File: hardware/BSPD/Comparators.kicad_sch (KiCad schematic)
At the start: 17 parts, among them U6 LM393, U7 LM393, U8 LM393, U9 74AHC1G32

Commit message: Crumbs of documentation added
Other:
- note added: "0.45V Out"
- note added: "Any voltage you desire out"
- note added: "Both comparators are set to detect braking within =< 30bar threshold; copied from previous BSPD Board"

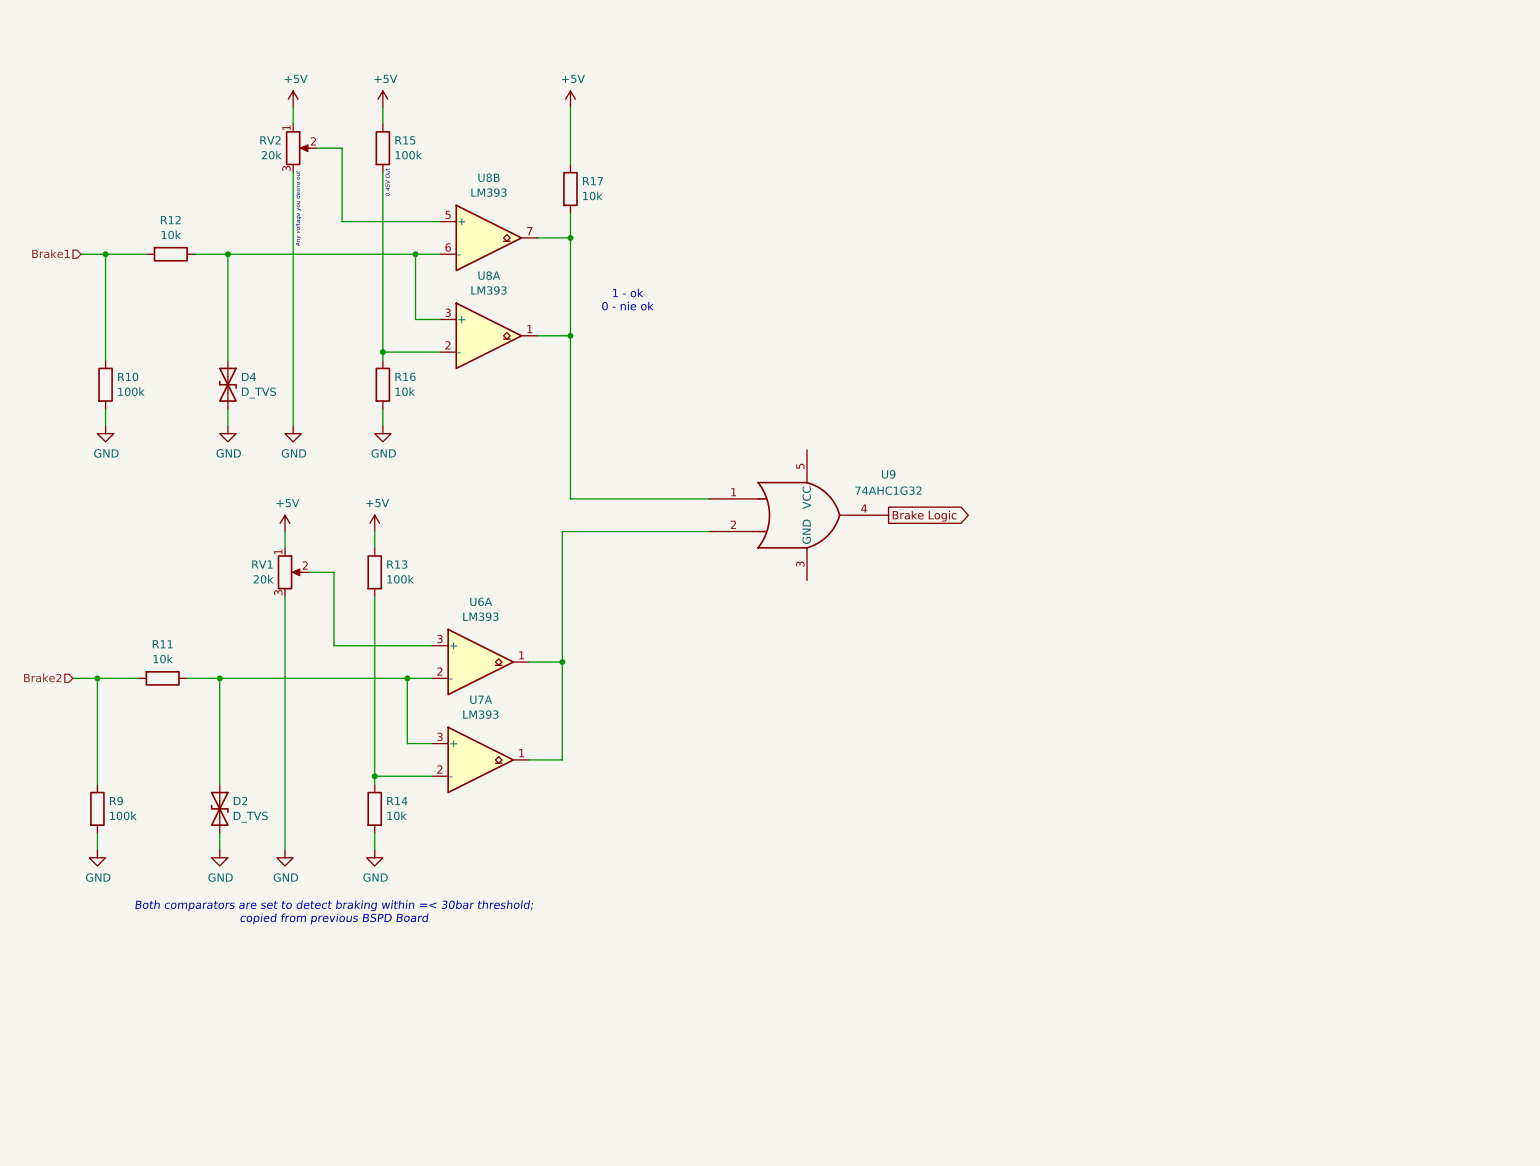
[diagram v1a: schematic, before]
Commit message: Timing Changed + Documented
Changed 10 second autoreset timer to a 555 in one-shot configuration. Also documented BSPD Board.
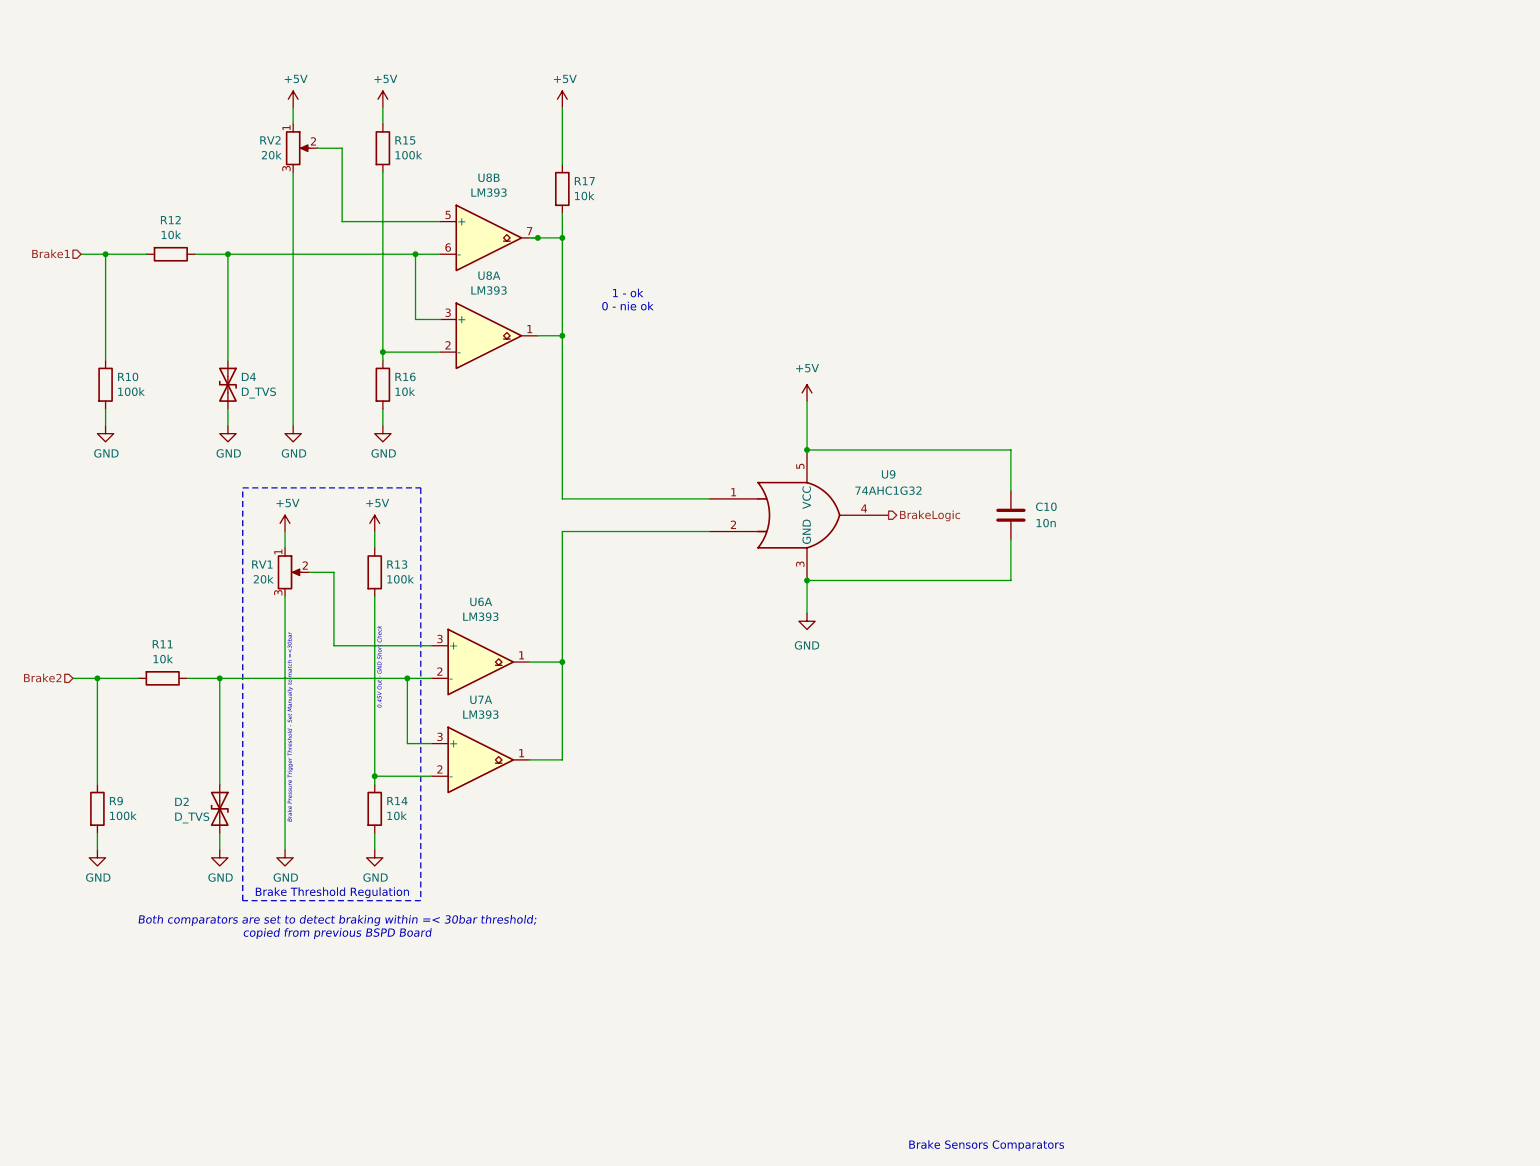
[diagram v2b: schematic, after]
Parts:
- added C10: 10n, symbol Device:C
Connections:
- net +5V: now also U9.5 (VCC), C10.1
- net GND: now also U9.3 (GND), C10.2
- net Brake Logic renamed BrakeLogic
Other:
- note added: "0.45V Out - GND Short Check"
- note added: "Brake Pressure Trigger Threshold - Set Manually to match =<30bar"
- note added: "Brake Sensors Comparators"
- note added: "Brake Threshold Regulation"
- note removed: "0.45V Out"
- note removed: "Any voltage you desire out"
- moved on the sheet: R17

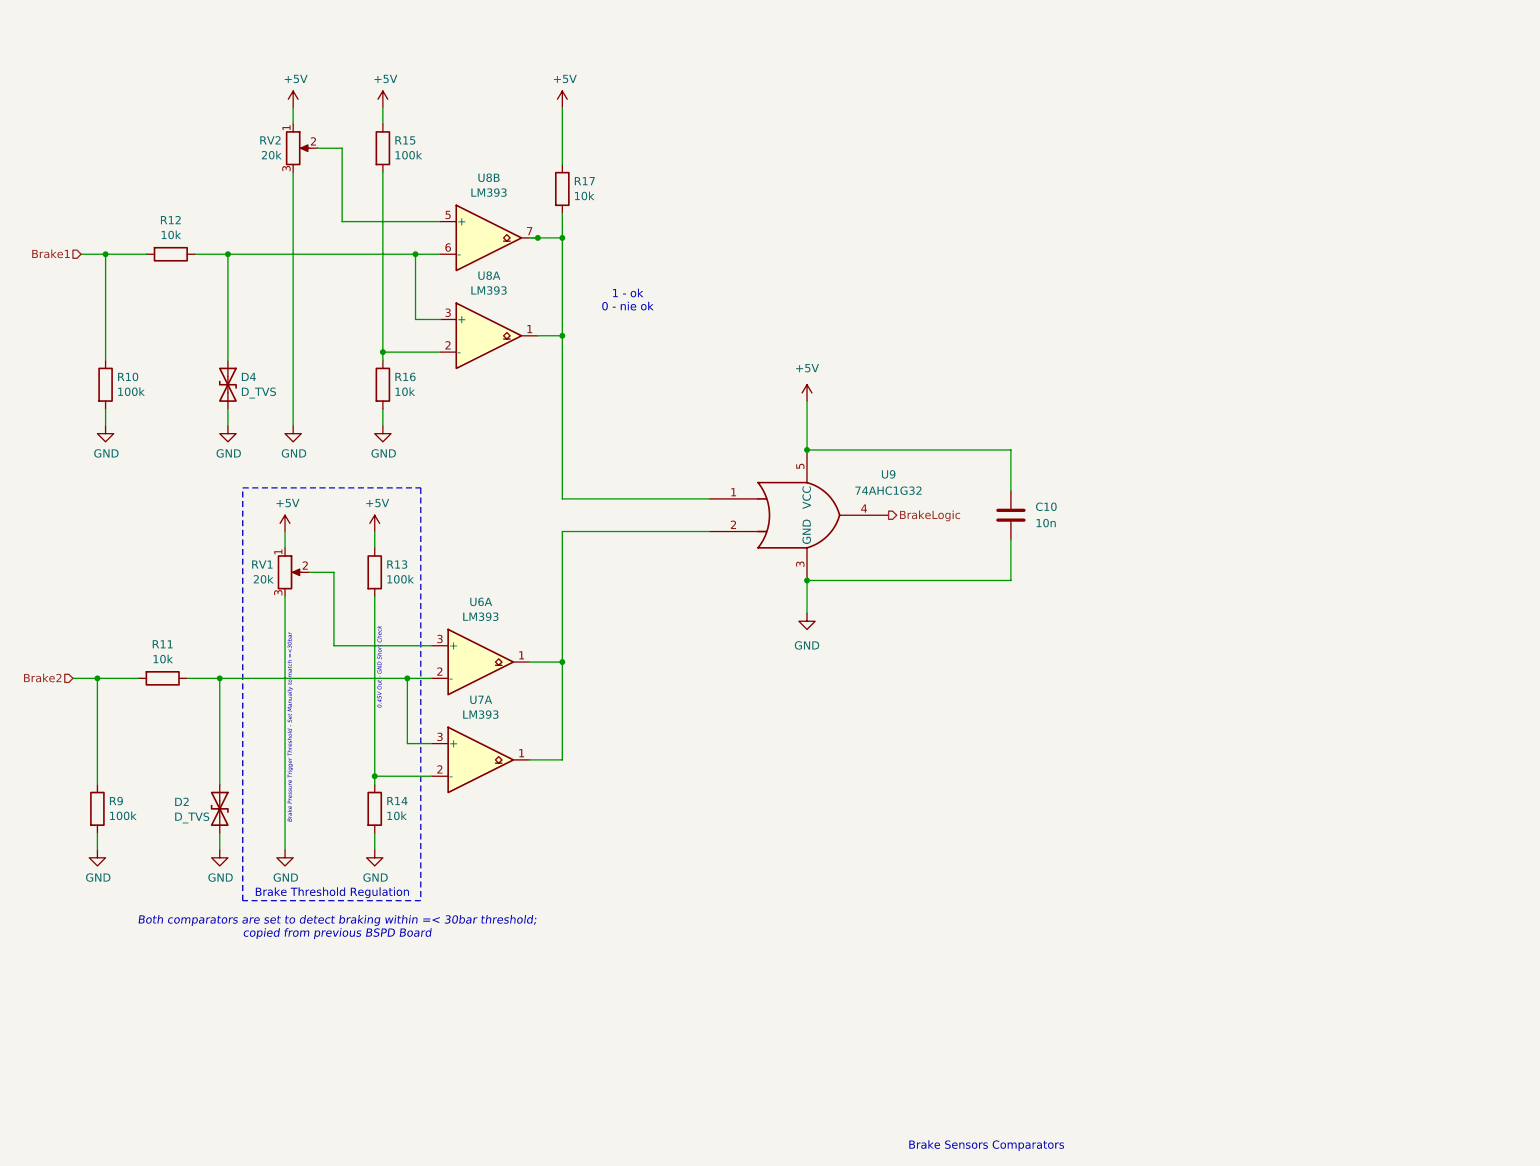
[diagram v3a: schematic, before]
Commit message: Fixed logic errors + assigned element values
Fixed wrong logic on Brake Sensor comparators, assigned IC's and connectors, added TVS diodes on connectors.
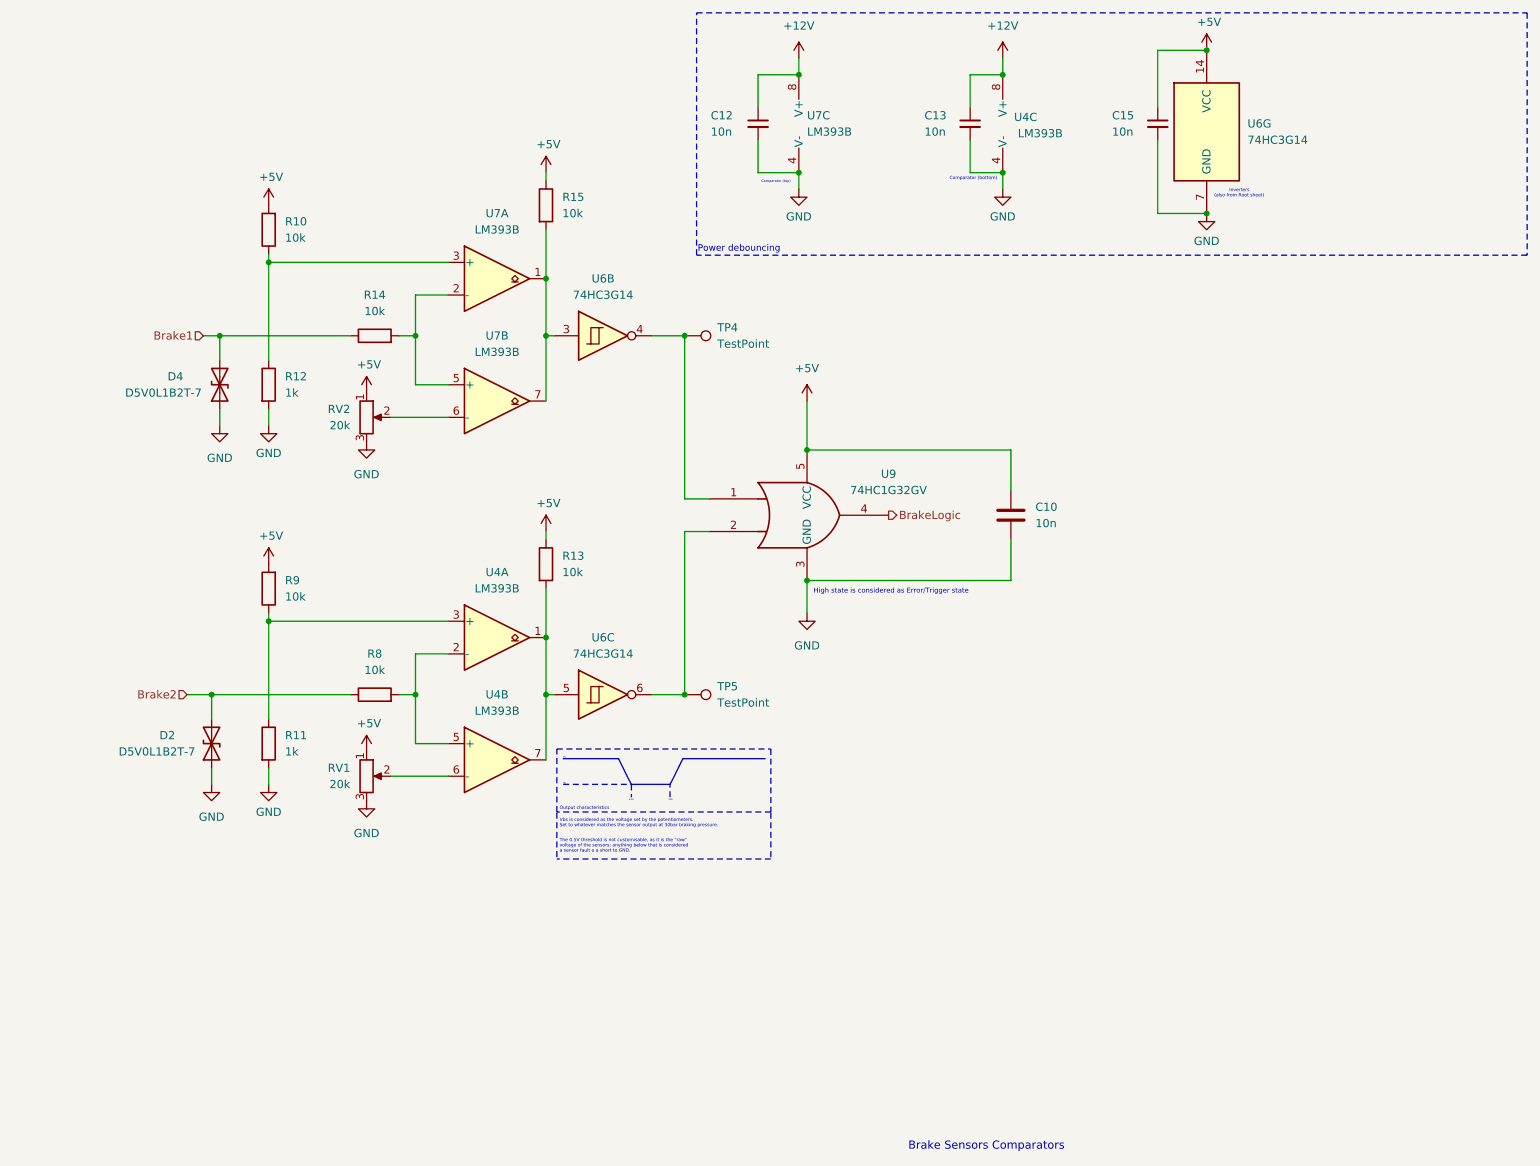
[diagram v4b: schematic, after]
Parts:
- removed R16, R17: 10k, Resistor_SMD:R_1206_3216Metric, symbol Device:R
- removed RV1, RV2: 20k, Potentiometer_THT:Potentiometer_ACP_CA9-H2,5_Horizontal, symbol Device:R_POT
- removed U6, U7, U8: LM393, Package_SO:SOIC-8_3.9x4.9mm_P1.27mm, symbol Comparator:LM393
- added C12, C13, C15: 10n, symbol Device:C_Small
- added R8: 10k, symbol Device:R
- added RV1, RV2: 20k, symbol Device:R_Potentiometer
- added TP4, TP5: TestPoint, symbol Connector:TestPoint
- added U4, U7: LM393B, symbol Comparator:MCP6567
- added U6: 74HC3G14, symbol 74xx:74HC14
- D2, D4: value D_TVS -> D5V0L1B2T-7; footprint Diode_SMD:D_SMB -> (none)
- R10, R13, R15, R9: value 100k -> 10k; footprint Resistor_SMD:R_1206_3216Metric -> (none)
- R11, R12: value 10k -> 1k; footprint Resistor_SMD:R_1206_3216Metric -> (none)
- R14: footprint Resistor_SMD:R_1206_3216Metric -> (none)
- U9: value 74AHC1G32 -> 74HC1G32GV
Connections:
- net +5V: now also R10.2, R9.2, C15.1, RV1.1, RV2.1, U6.14 (VCC)
- net Brake1: now also D4.2 (A2), R14.1; no longer R10.1, R12.2
- net Brake2: now also D2.2 (A2), R8.1; no longer R11.2, R9.1
- net GND: now also D2.1 (A1), D4.1 (A1), R11.2, R12.2, C12.2, C13.2, C15.2, RV1.3, RV2.3, U4.4 (V-), U6.7 (GND), U7.4 (V-); no longer D2.2 (A2), D4.2 (A2), R10.2, R14.2, R9.2
- net at R11.1: now also R9.1, U4.3 (+); no longer D2.1 (A1)
- net at U9.1: now also TP4.1, U6.4
- net at R15.2: now also U6.3, U7.1, U7.7
- net at R12.1: now also R10.1, U7.3 (+); no longer D4.1 (A1)
- net at U9.2: now also TP5.1, U6.6
- net at R13.2: now also U4.1, U4.7, U6.5; no longer R14.1
- new net: R14.2, U7.2 (-), U7.5 (+)
- new net: R8.2, U4.2 (-), U4.5 (+)
- new net: RV2.2, U7.6 (-)
- new net: RV1.2, U4.6 (-)
- new net +12V: C12.1, C13.1, U4.8 (V+), U7.8 (V+)
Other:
- note added: "0.5V"
- note added: "0V"
- note added: "5V"
- note added: "Comparator (bottom)"
- note added: "Comparator (top)"
- note added: "High state is considered as Error/Trigger state"
- note added: "Inverters (also from Root sheet)"
- note added: "Output characteristics"
- note added: "Power debouncing"
- note added: "The 0.5V threshold is not customisable, as it is the "raw" voltage of the sensors; anything below that is considered a sensor fault o a short to GND."
- note added: "Vbs"
- note added: "Vbs is considered as the voltage set by the potentiometers. Set to whatever matches the sensor output at 30bar braking pressure."
- note removed: "0.45V Out - GND Short Check"
- note removed: "1 - ok 0 - nie ok"
- note removed: "Both comparators are set to detect braking within =< 30bar threshold; copied from previous BSPD Board"
- note removed: "Brake Pressure Trigger Threshold - Set Manually to match =<30bar"
- note removed: "Brake Threshold Regulation"

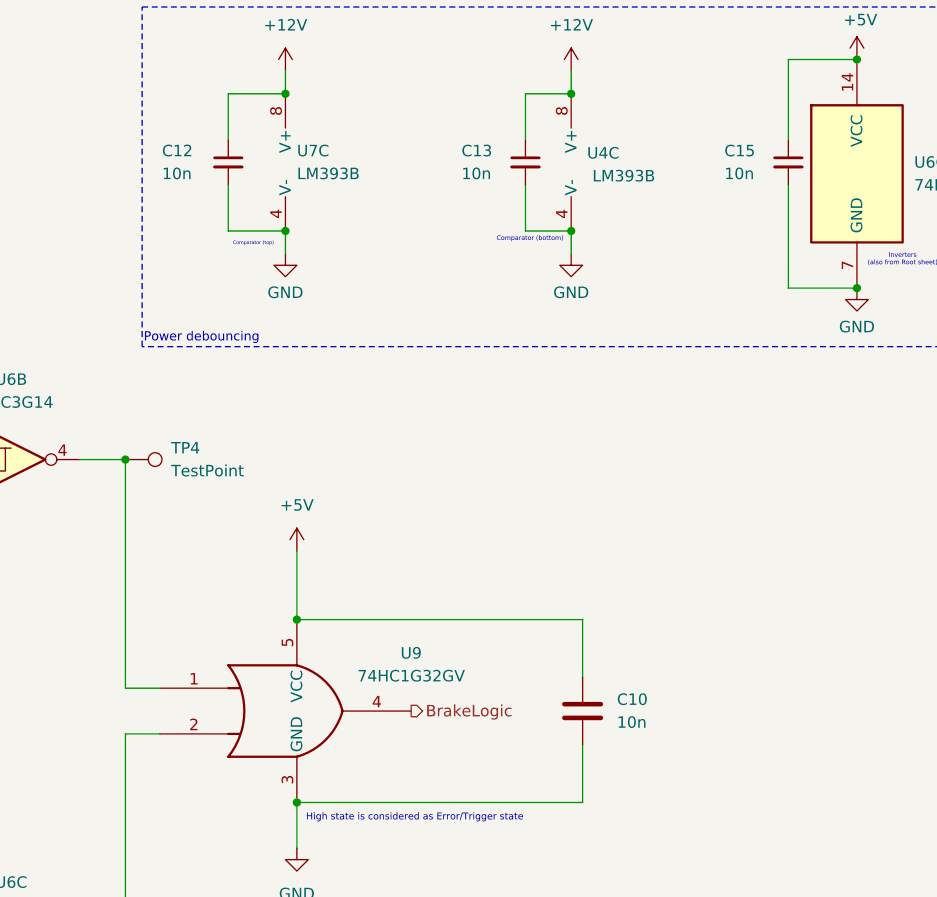
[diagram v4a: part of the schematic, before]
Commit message: Fixed 555 configuration + power debouncing
Changed power debouncing capacitors to 100nF
Fixed the One-Shot 555
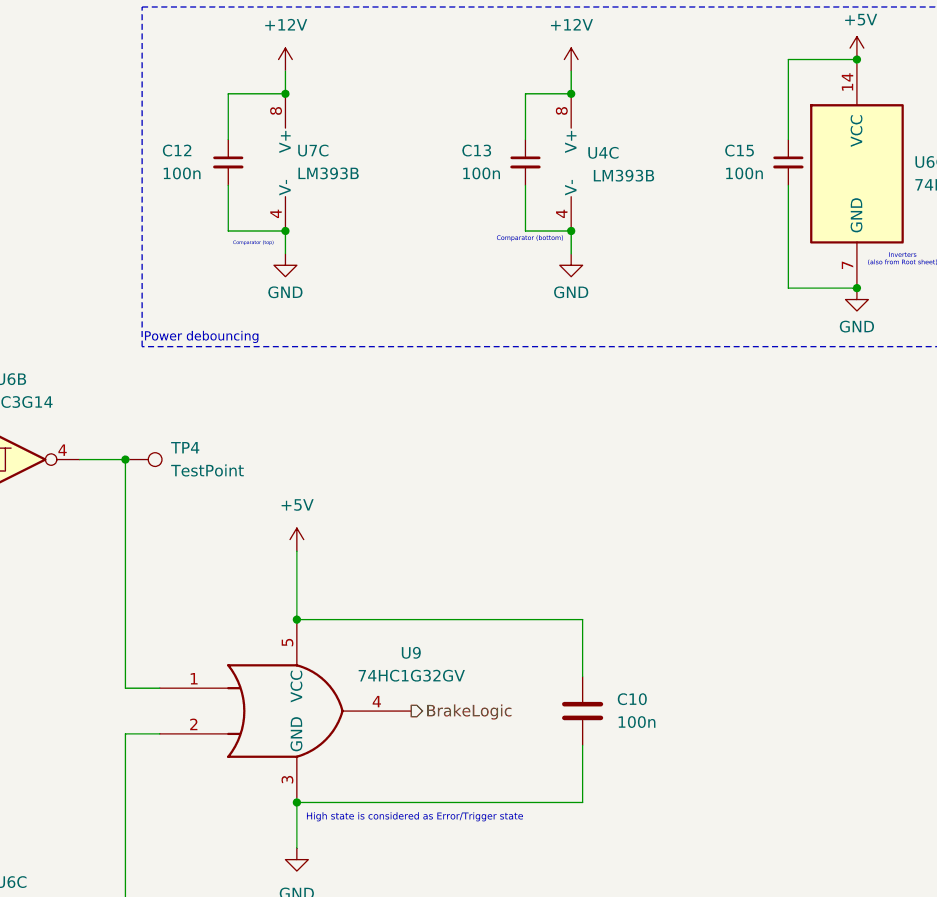
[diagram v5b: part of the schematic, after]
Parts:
- C10, C12, C13, C15: value 10n -> 100n
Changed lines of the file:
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@@
 			)
 		)
-		(property "Value" "10n"
+		(property "Value" "100n"
 			(at 156.464 31.75 0)
 			(effects
@@
 			)
 		)
-		(property "Value" "10n"
+		(property "Value" "100n"
 			(at 189.738 31.75 0)
 			(effects
@@
 			)
 		)
-		(property "Value" "10n"
+		(property "Value" "100n"
 			(at 218.948 31.75 0)
 			(effects
@@
 			)
 		)
-		(property "Value" "10n"
+		(property "Value" "100n"
 			(at 207.01 92.7099 0)
 			(effects

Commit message: Fixed Comparators
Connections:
- net at R10.1, R12.1: now also U7.6 (-); no longer U7.3 (+)
- net at R11.1, R9.1: now also U4.6 (-); no longer U4.3 (+)
- net at RV2.2: now also U7.3 (+); no longer U7.6 (-)
- net at RV1.2: now also U4.3 (+); no longer U4.6 (-)
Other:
- moved on the sheet: R12, RV1, RV2
